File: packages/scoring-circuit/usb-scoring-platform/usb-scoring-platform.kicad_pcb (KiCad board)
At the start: 4 copper layers, 160 x 100 mm, 151 parts, among them J1 GCT USB4105-GF-A, J10 5520250-2, J2 STM SWD 3.3V, J3 LEFT WEAPON A B C, J4 RIGHT WEAPON A B C, J5 PISTE - NOT protective earth, J6 ESP 3.3V UART recovery, J7 TST-108-02-G-D - HUB75, J8 645004114822 - panel 5V, J9 5520250-2, Q1 BSS138-7-F, Q2 BSS138-7-F, Q3 BSS138-7-F, SW1 STM RESET, SW2 ESP RESET, SW3 ESP BOOT, U1 STM32G474RET6, U10 SN74AXC1T45DCKR, U11 SN74AXC1T45DCKR, U12 WIZ850io, U13 TSOP38438, U14 SN74AHCT245PWR, U15 SN74AHCT245PWR, U16 4N32M, U17 4N32M, U18 LTM2884IY#PBF, U2 ESP32-S3-WROOM-1-N8R8, U3 USBLC6-2SC6, U4 AP2112K-3.3TRG1, U5 Adafruit 5807 - set 20V, U6 D36V50F5, U7 AP63203WU-7, U8 74LVC125APW, U9 74LVC125APW, Y1 ABM3B-8.000MHZ-B2-T

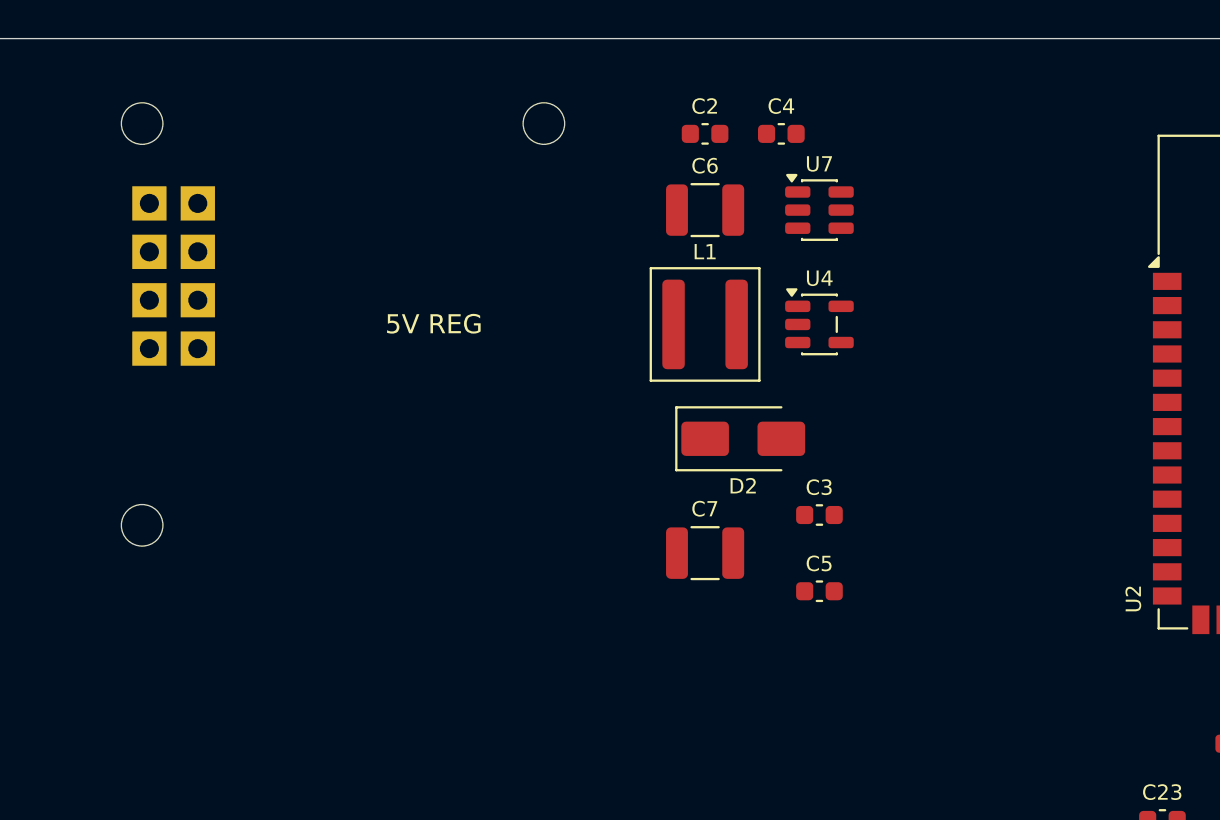
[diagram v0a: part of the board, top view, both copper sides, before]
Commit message: feat(scoring-circuit): route application buck power section
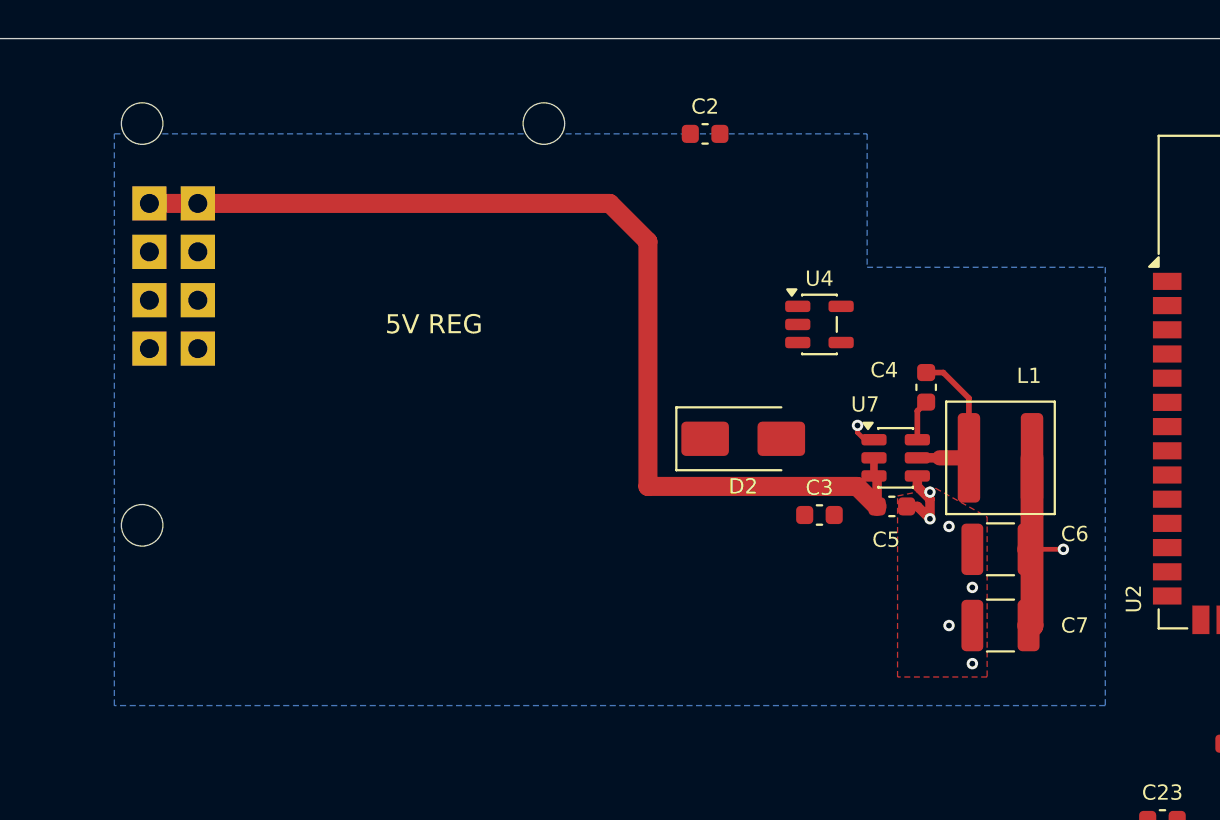
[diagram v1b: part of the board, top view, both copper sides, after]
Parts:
- moved C6 23.6 mm to (128.5, 76.8), turned to 180 degrees
- moved L1 17.0 mm to (128.5, 72.0)
- moved C7 16.0 mm to (128.5, 80.8), turned to 180 degrees
- moved C4 15.3 mm to (124.6, 68.3), turned to 90 degrees
- moved U7 13.6 mm to (123.0, 72.0)
- moved C5 5.85 mm to (122.8, 74.5)
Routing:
- net PANEL_5V: track 0.00 -> 54.9 mm
- net APP_3V3: track 0.00 -> 27.3 mm, vias 0 -> 2
- net BUCK_SW: track 0.00 -> 8.64 mm
- net GND: track 0.00 -> 4.02 mm, vias 0 -> 6
- net BUCK_BOOT: track 0.00 -> 2.17 mm
- added copper zone on B.Cu, net GND
- added copper zone on F.Cu, net GND
- added copper zone on In1.Cu, net GND
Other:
- board text added: "USB SCORING PLATFORM - ROUTING IN PROGRESS - NOT FOR FABRICATION"
- board text removed: "USB SCORING PLATFORM - UNROUTED ENGINEERING DRAFT"

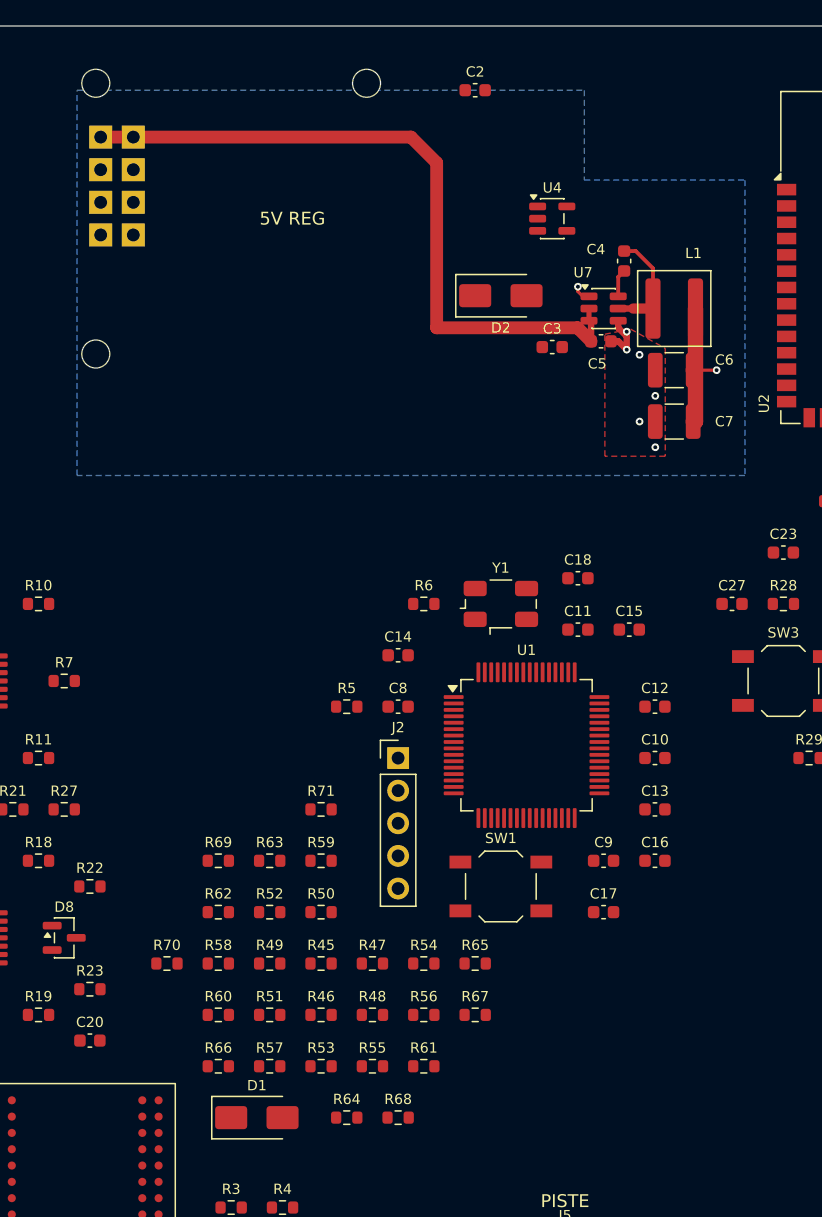
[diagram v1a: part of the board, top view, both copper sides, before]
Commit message: feat(scoring-circuit): route STM32 supply and decoupling
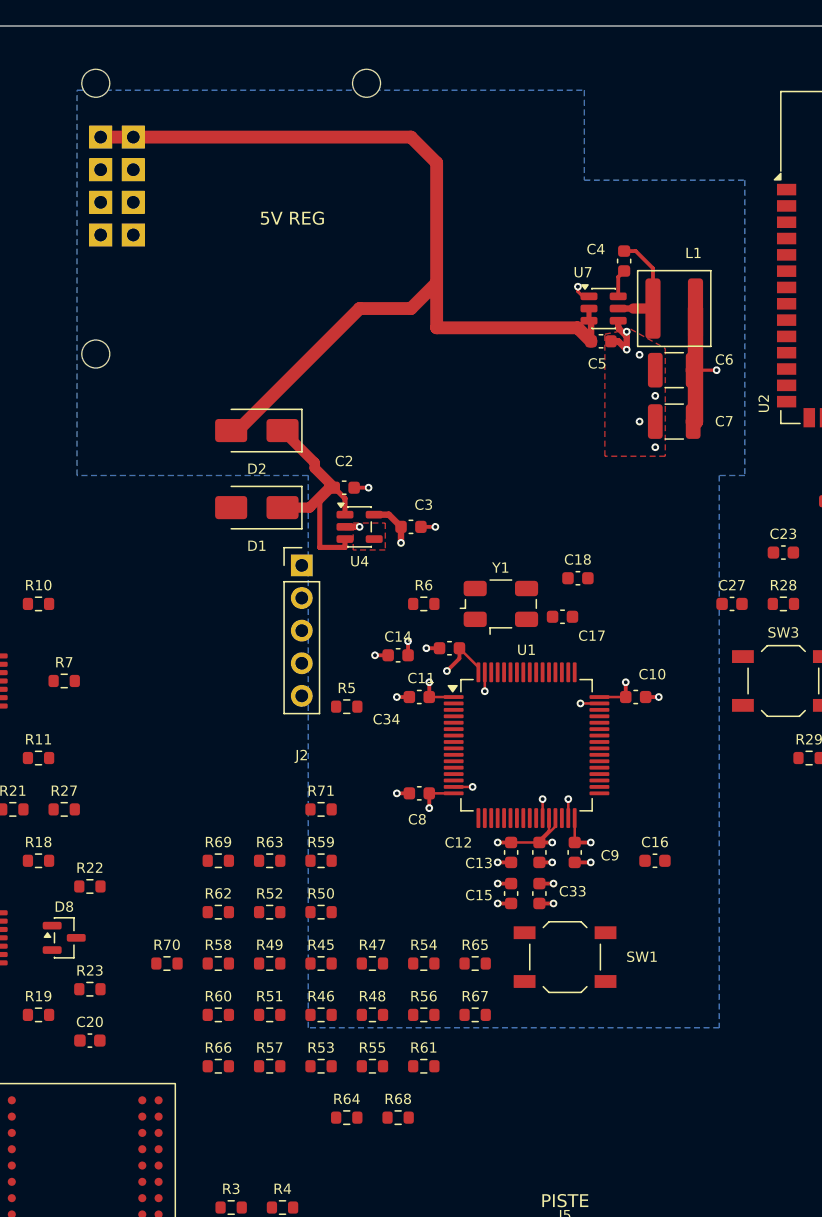
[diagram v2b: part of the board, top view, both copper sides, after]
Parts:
- added C33: 1uF 10V, Capacitor_SMD:C_0603_1608Metric, F.Cu at (118.0, 117.5)
- added C34: 100nF 10V, Capacitor_SMD:C_0603_1608Metric, F.Cu at (108.7, 102.2)
- C12: value 100nF 10V -> 10nF 10V
- moved D1 47.5 mm to (96.0, 87.5), turned to 180 degrees
- moved C2 32.6 mm to (102.8, 86.0)
- moved U4 28.3 mm to (104.0, 89.0)
- moved C17 23.2 mm to (119.8, 96.0)
- moved C15 22.5 mm to (115.8, 117.5), turned to -90 degrees
- moved D2 21.7 mm to (96.0, 81.5), turned to 180 degrees
- moved C3 17.8 mm to (108.0, 89.0)
- moved J2 16.8 mm to (99.5, 92.0)
- moved C12 14.5 mm to (118.0, 114.3), turned to -90 degrees
- moved C13 11.7 mm to (115.8, 114.3), turned to -90 degrees
- moved C11 10.1 mm to (111.0, 98.5), turned to 180 degrees
- moved SW1 7.43 mm to (120.0, 122.5)
- moved C8 6.95 mm to (108.7, 109.8), turned to 180 degrees
- moved C10 4.98 mm to (125.5, 102.2)
- moved C9 2.34 mm to (120.8, 114.3), turned to -90 degrees
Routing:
- net CORE_3V3: track 0.00 -> 44.9 mm, vias 0 -> 11
- net GND: track 4.02 -> 25.3 mm, vias 6 -> 24
- net CORE_5V: track 0.00 -> 21.0 mm
- net PANEL_5V: track 54.9 -> 75.7 mm
- added copper zone on In2.Cu, net CORE_3V3

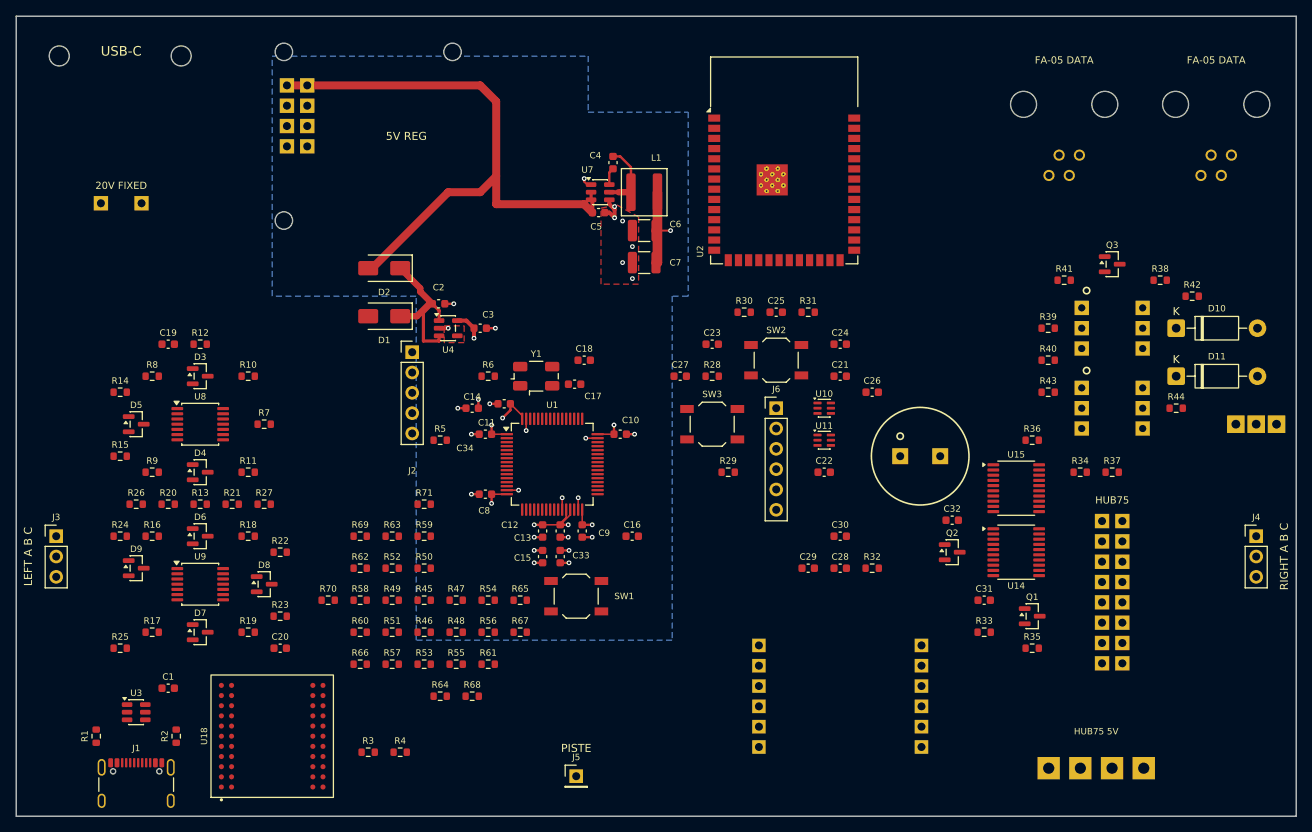
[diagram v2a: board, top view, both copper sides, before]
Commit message: feat(scoring-circuit): route isolated USB power and data
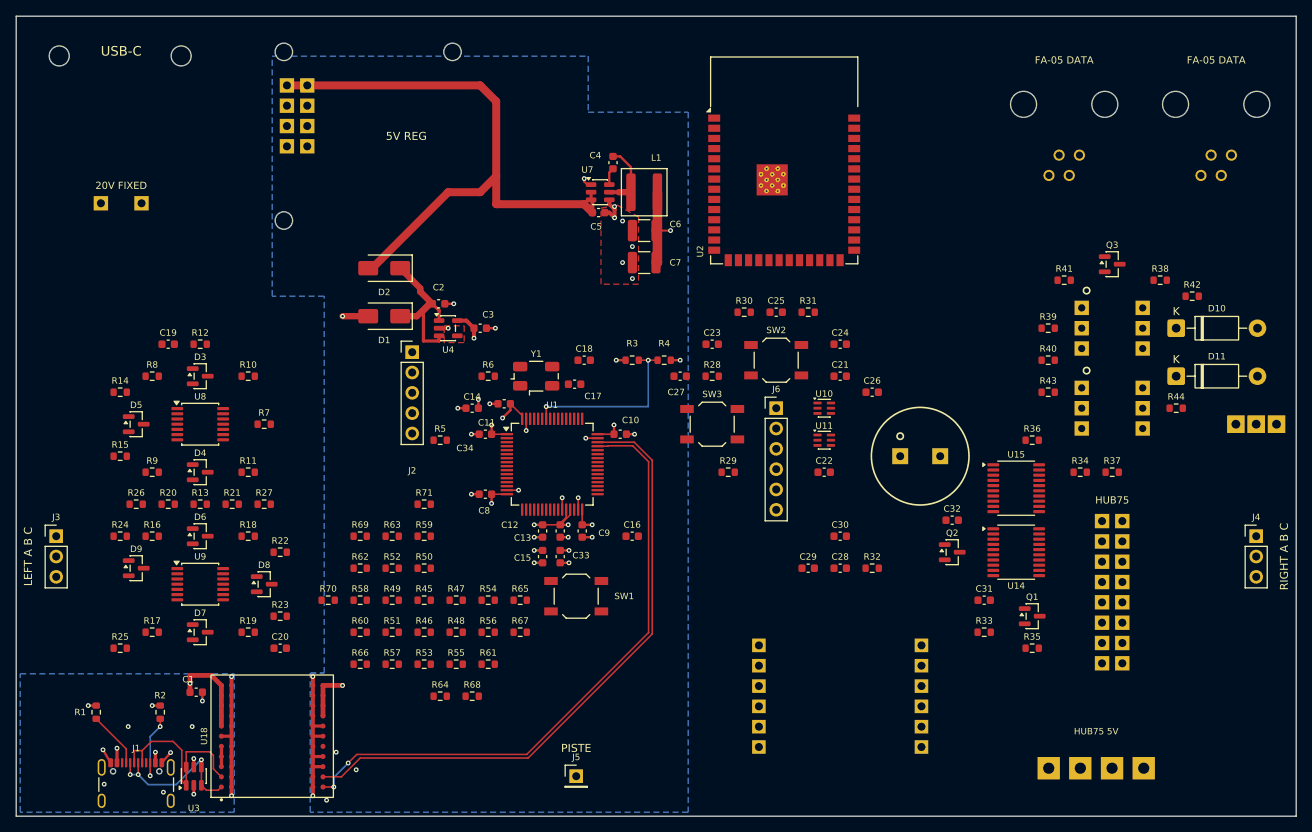
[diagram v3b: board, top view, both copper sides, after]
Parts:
- moved R3 59.1 mm to (127.0, 93.0)
- moved R4 59.1 mm to (131.0, 93.0)
- moved U3 10.8 mm to (72.2, 145.0), turned to 90 degrees
- moved R2 3.61 mm to (68.0, 137.0)
- moved C1 3.54 mm to (72.5, 134.5)
- moved R1 3.00 mm to (60.0, 137.0)
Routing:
- net USB_ISOLATED_5V: track 0.00 -> 95.6 mm, vias 0 -> 3
- net USB_DP: track 0.00 -> 78.0 mm
- net USB_DM: track 0.00 -> 78.0 mm, vias 0 -> 2
- net USB_VBUS: track 0.00 -> 55.9 mm, vias 0 -> 4
- net USB_HOST_DP: track 0.00 -> 25.4 mm
- net USB_GND: track 0.00 -> 23.9 mm, vias 0 -> 12
- net USB_PRESENT: track 0.00 -> 22.4 mm, vias 0 -> 2
- net GND: track 25.3 -> 46.5 mm, vias 24 -> 30
- net USB_HOST_DM: track 0.00 -> 19.8 mm, vias 0 -> 3
- net USB_CC2: track 0.00 -> 9.27 mm, vias 0 -> 2
- net USB_CC1: track 0.00 -> 7.05 mm
- net USB_HOST_3V3: track 0.00 -> 2.54 mm
- added copper zone on In2.Cu, net GND
- added copper zone on B.Cu, net USB_GND
- added copper zone on In1.Cu, net USB_GND
- added copper zone on In2.Cu, net USB_GND

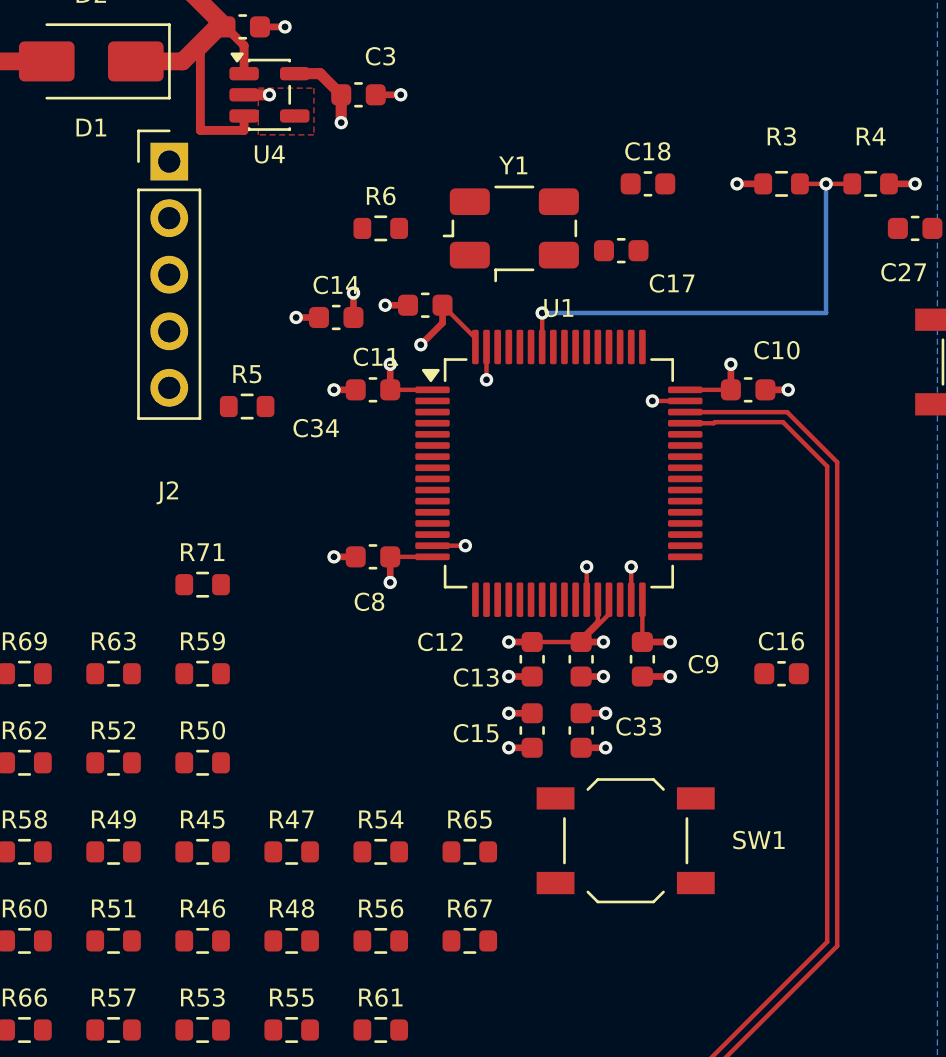
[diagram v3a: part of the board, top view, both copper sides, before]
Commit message: feat(scoring-circuit): route STM32 clock reset and programming
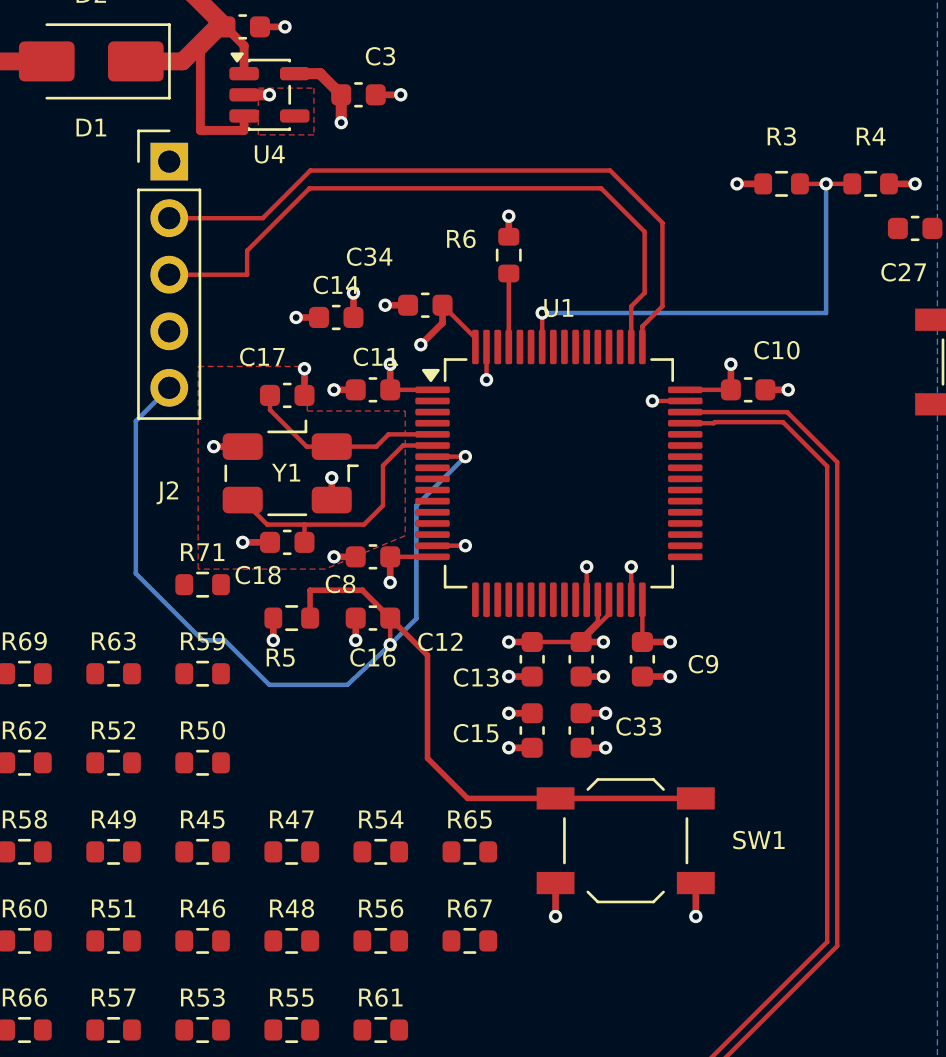
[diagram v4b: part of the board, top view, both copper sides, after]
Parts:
- moved C18 22.8 mm to (104.8, 109.1), turned to 180 degrees
- moved C16 18.5 mm to (108.7, 112.5), turned to 180 degrees
- moved C17 16.3 mm to (104.8, 102.5)
- moved Y1 15.0 mm to (104.8, 106.0), turned to 180 degrees
- moved R5 9.71 mm to (105.0, 112.5)
- moved R6 5.87 mm to (114.8, 96.2), turned to 90 degrees
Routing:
- net STM_RESET_N: track 0.00 -> 60.8 mm, vias 0 -> 2
- net SWDIO: track 0.00 -> 30.0 mm
- net SWCLK: track 0.00 -> 29.8 mm
- net CORE_3V3: track 44.9 -> 60.3 mm, vias 11 -> 12
- net HSE_OUT: track 0.00 -> 12.3 mm
- net GND: track 46.5 -> 56.1 mm, vias 30 -> 38
- net HSE_IN: track 0.00 -> 8.86 mm
- net STM_BOOT0: track 0.00 -> 3.30 mm
